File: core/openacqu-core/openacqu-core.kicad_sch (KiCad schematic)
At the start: 30 parts, among them J1 GSB1C41110SSHR, U1 MCP2221AT-I_ML, U2 LP5817DRLR, U3 FXL6408UMX, U4 24AA025E48T-E_OT, U5 AP2112K-3.3TRG1, U6 TPS22996HQDYCRQ1

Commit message: Core placement and 3D models
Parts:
- removed C5: 1uF, CL05A105KO5NNNC:CAPC1005X55N, symbol CL05A105KO5NNNC:CL05A105KO5NNNC
- added H1, H2, H3, H4: M3, MountingHole:MountingHole_3.5mm_Pad, symbol Mechanical:MountingHole_Pad
- C1, C2, C3, C4, C6, C7, C8, C9: footprint CL05A105KO5NNNC:CAPC1005X55N -> openacqu_footprints:CAPC1005X55N
- D1: footprint WL-SFTW_3528_PLCC4:WL-SFTW_3528_PLCC4 -> openacqu_footprints:WL-SFTW_3528_PLCC4
- D2, D4: footprint ESD321DPYR:TVS_ESD321DPYR -> openacqu_footprints:TVS_ESD321DPYR
- D3: footprint PESD5V0X1UB:SOD523 -> openacqu_footprints:SOD523
- J1: footprint GSB1C41110SSHR:AMPHENOL_GSB1C41110SSHR -> openacqu_footprints:AMPHENOL_GSB1C41110SSHR
- R1, R2, R7, R8: footprint RC0402FR-075K1L:RESC1005X40N -> openacqu_footprints:RESC1005X40N
- R10, R3, R4, R5, R6, R9: footprint RC0402FR-0710KL:RESC1005X40N -> openacqu_footprints:RESC1005X40N
- U2: footprint LP5817DRLR:IC_LP5817DRLR -> openacqu_footprints:IC_LP5817DRLR
- U3: footprint FXL6408UMX:QFN40P260X180X55-16N -> openacqu_footprints:QFN40P260X180X55-16N
- U4: footprint 24AA025E48T-E_OT:SOT95P270X145-6N -> openacqu_footprints:SOT95P270X145-6N
- U5: footprint AP2112K-3.3TRG1:SOT95P285X140-5N -> openacqu_footprints:SOT95P285X140-5N
- U6: footprint TPS22996HQDYCRQ1:IC_TPS22996HQDYCRQ1 -> openacqu_footprints:IC_TPS22996HQDYCRQ1
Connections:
- net GND: now also H1.1, H2.1, H3.1, H4.1
- net ON1: now reaches R3.2, U6.1 (ON1)
- net ON2: now reaches R4.2, U6.4 (ON2)
- net CC1: now reaches J1.A5 (CC1), R2.1
- net CC2: now reaches J1.B5 (CC2), R1.1
- net FX_INT: now reaches R5.2, U3.1 (~{INT})
- net MCP_RST: now reaches R10.2, U1.3 (~{RST})
- net LED_B: now reaches U2.6 (OUT2)
- net LED_B: now also D1.2; no longer D1.4
- net LED_R: now reaches D1.3, U2.7 (OUT1)
- net LED_G: now reaches U2.8 (OUT0)
- net LED_G: now also D1.4; no longer D1.2
- net FX_RST: now reaches R6.2, U3.10 (~{RST})
- net MCP_URX: now reaches R9.1, U1.4 (URX)
- no-connect marks 16 -> 18
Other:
- moved on the sheet: C4, C6, D1, R10, R3, R4, R9, U6

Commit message: Routed core design
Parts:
- added C5: 1uF, openacqu_footprints:CAPC1005X55N, symbol CL05A105KO5NNNC:CL05A105KO5NNNC
- added J2: Test Points, openacqu_footprints:MLE_TSHC-110-S-14-295-G-LF, symbol TSHC-110-S-14-295-G-LF:TSHC-110-S-14-295-G-LF
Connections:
- net +3V3: now also C5.1, J2.09
- net +3V3_SYS: now also J2.04
- net +5V0_SYS: now also J2.03
- net GND: now also C5.2, J2.02, J2.08
- net LED_G: now also U2.7 (OUT1); no longer U2.8 (OUT0)
- net LED_R: now also U2.8 (OUT0); no longer U2.7 (OUT1)
- net SCL: now also J2.07
- net SDA: now also J2.05, J2.06
- net VBUS: now also J2.10
- no-connect marks 18 -> 19
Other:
- moved on the sheet: C8, C9, R10, R5, R6, R7, R8, R9, U1, U3

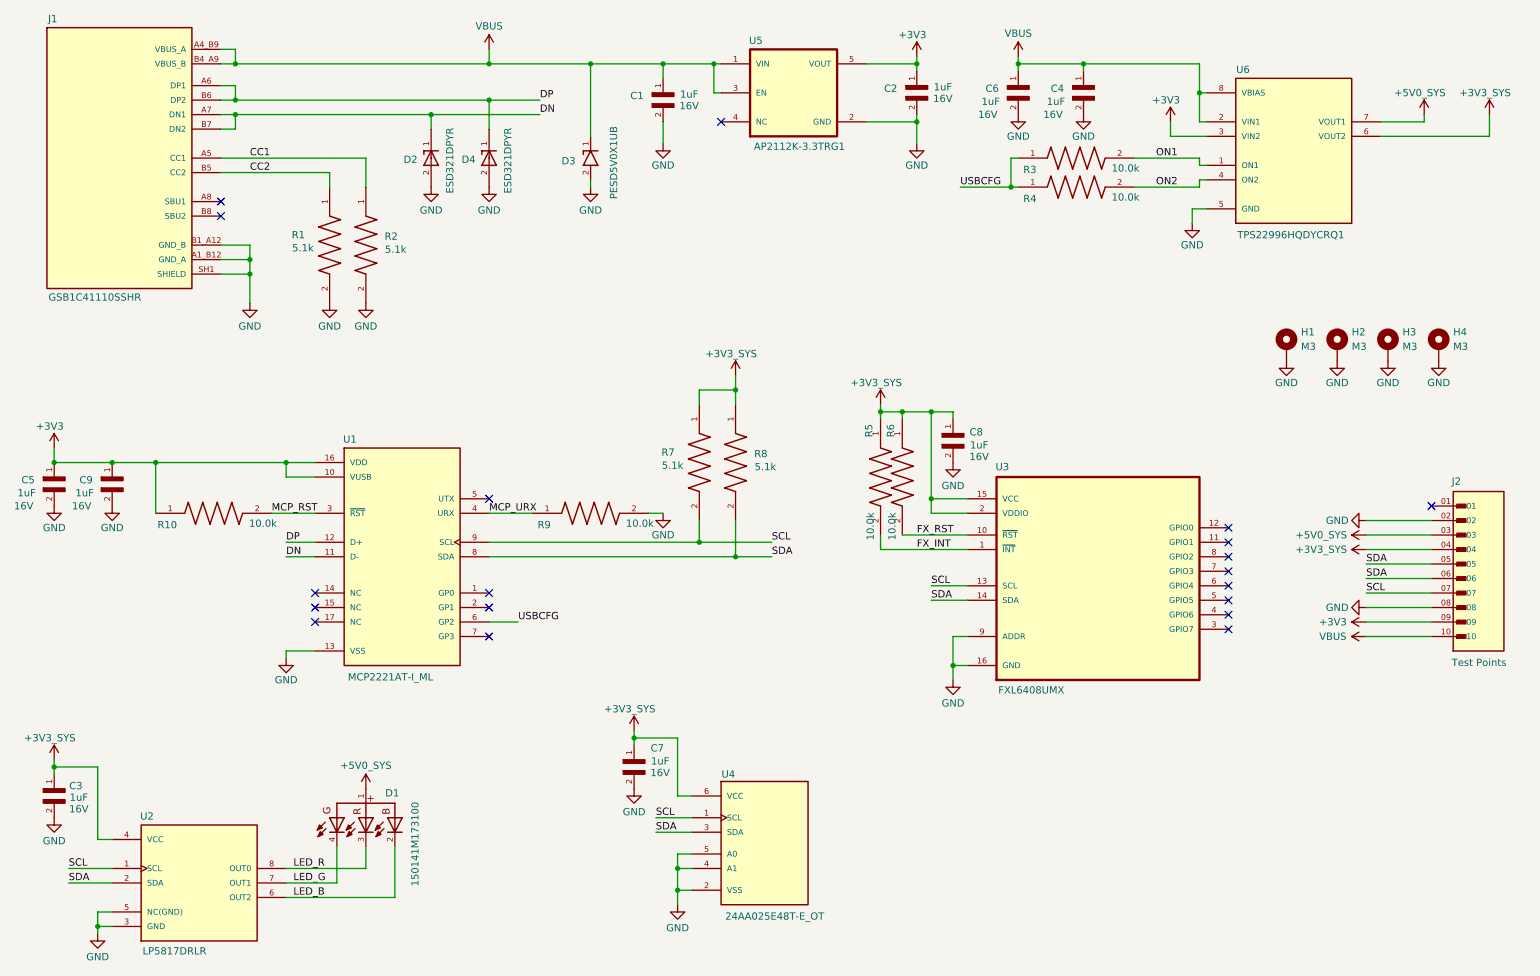
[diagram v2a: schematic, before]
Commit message: Moved core to separate sheet
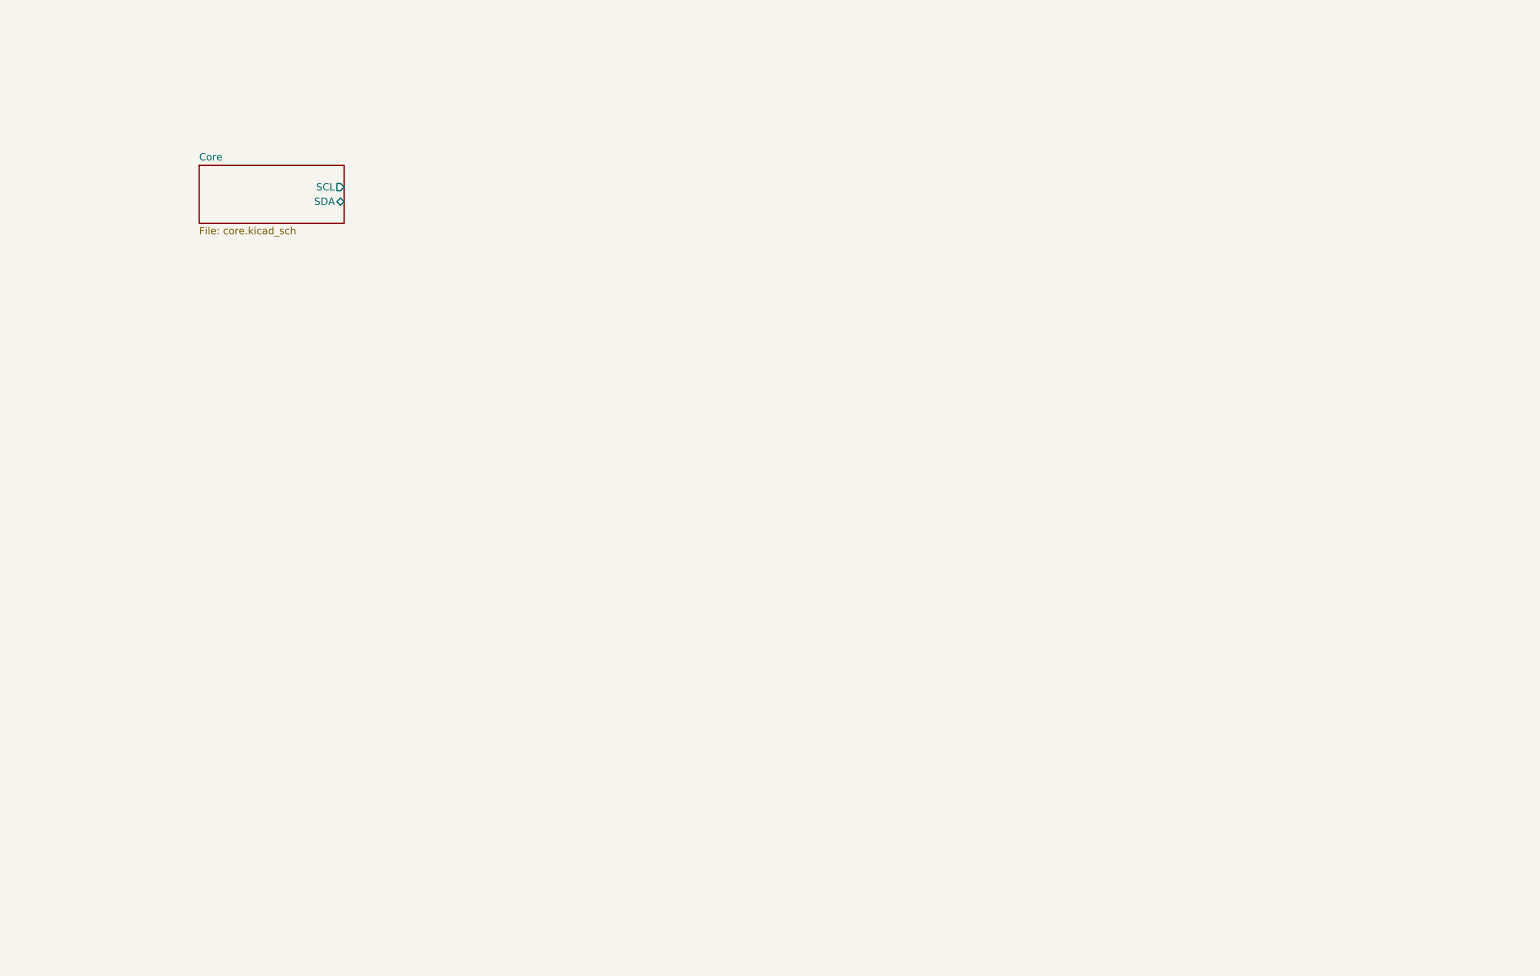
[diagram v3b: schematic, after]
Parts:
- removed C1, C2, C3, C4, C5, C6, C7, C8, C9: 1uF, openacqu_footprints:CAPC1005X55N, symbol CL05A105KO5NNNC:CL05A105KO5NNNC
- removed D1: 150141M173100, openacqu_footprints:WL-SFTW_3528_PLCC4, symbol WL-SFTW_3528_PLCC4:WL-SFTW_3528_PLCC4
- removed D2, D4: ESD321DPYR, openacqu_footprints:TVS_ESD321DPYR, symbol ESD321DPYR:ESD321DPYR
- removed D3: PESD5V0X1UB, openacqu_footprints:SOD523, symbol PESD5V0X1UB:PESD5V0X1UB
- removed H1, H2, H3, H4: M3, MountingHole:MountingHole_3.5mm_Pad, symbol Mechanical:MountingHole_Pad
- removed J1: GSB1C41110SSHR, openacqu_footprints:AMPHENOL_GSB1C41110SSHR, symbol GSB1C41110SSHR:GSB1C41110SSHR
- removed J2: Test Points, openacqu_footprints:MLE_TSHC-110-S-14-295-G-LF, symbol TSHC-110-S-14-295-G-LF:TSHC-110-S-14-295-G-LF
- removed R1, R2, R7, R8: 5.1k, openacqu_footprints:RESC1005X40N, symbol RC0402FR-075K1L:RC0402FR-075K1L
- removed R10, R3, R4, R5, R6, R9: 10.0k, openacqu_footprints:RESC1005X40N, symbol RC0402FR-0710KL:RC0402FR-0710KL
- removed U1: MCP2221AT-I_ML, openacqu_footprints:MCP2221AT-I_ML, symbol MCP2221AT-I_ML:MCP2221AT-I_ML
- removed U2: LP5817DRLR, openacqu_footprints:IC_LP5817DRLR, symbol LP5817DRLR:LP5817DRLR
- removed U3: FXL6408UMX, openacqu_footprints:QFN40P260X180X55-16N, symbol FXL6408UMX:FXL6408UMX
- removed U4: 24AA025E48T-E_OT, openacqu_footprints:SOT95P270X145-6N, symbol 24AA025E48T-E_OT:24AA025E48T-E_OT
- removed U5: AP2112K-3.3TRG1, openacqu_footprints:SOT95P285X140-5N, symbol AP2112K-3.3TRG1:AP2112K-3.3TRG1
- removed U6: TPS22996HQDYCRQ1, openacqu_footprints:IC_TPS22996HQDYCRQ1, symbol TPS22996HQDYCRQ1:TPS22996HQDYCRQ1
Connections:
- no-connect marks 19 -> 0
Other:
- added sheet Core (core.kicad_sch)
